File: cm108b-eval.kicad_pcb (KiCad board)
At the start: 2 copper layers, 60 x 50 mm, 42 parts, among them IC1 CM108B, J1 SPKR, J2 MIC, J3 RADIO_DATA, SW1 MUTE_REC, SW2 MUTE_PLAY, SW3 VOL_DN, SW4 VOL_UP

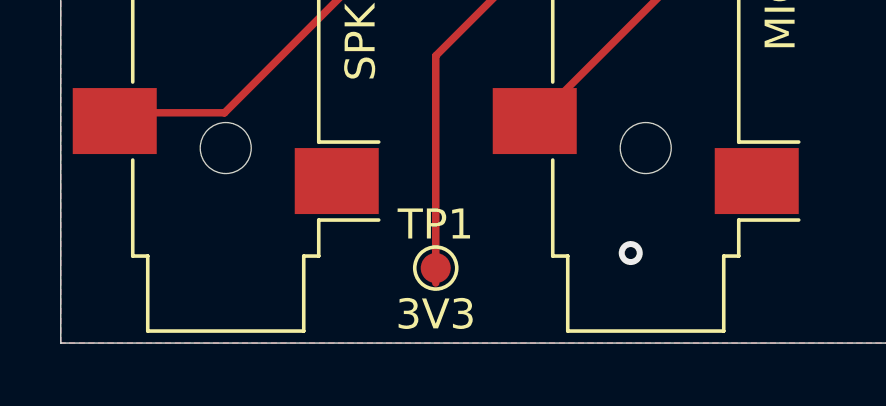
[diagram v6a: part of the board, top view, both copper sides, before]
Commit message: Fix USB connector from A to micro-B
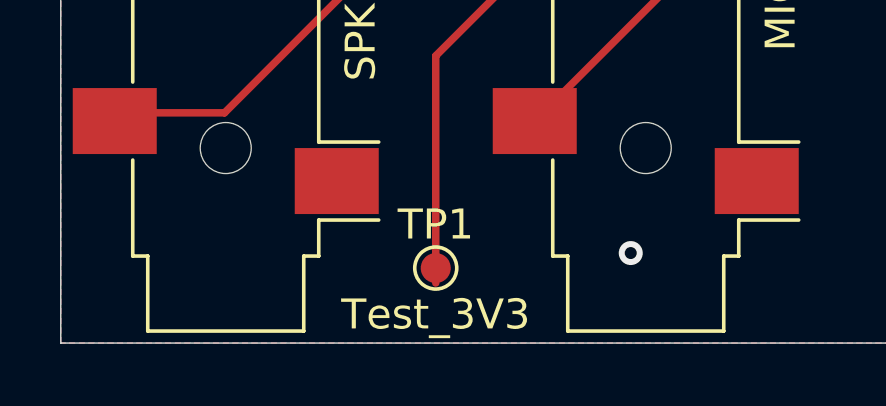
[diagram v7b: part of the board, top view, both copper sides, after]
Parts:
- JP2: value USB_A -> USB_MICRO_B
- TP1: value 3V3 -> Test_3V3
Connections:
- JP2 pad 4: GND -> (no net)
- JP2 pad 5: Net-(JP2-Pad5) -> GND
- JP2 pad 6: (no net) -> Net-(JP2-Pad6)
- L2 pad 2: Net-(JP2-Pad5) -> Net-(JP2-Pad6)

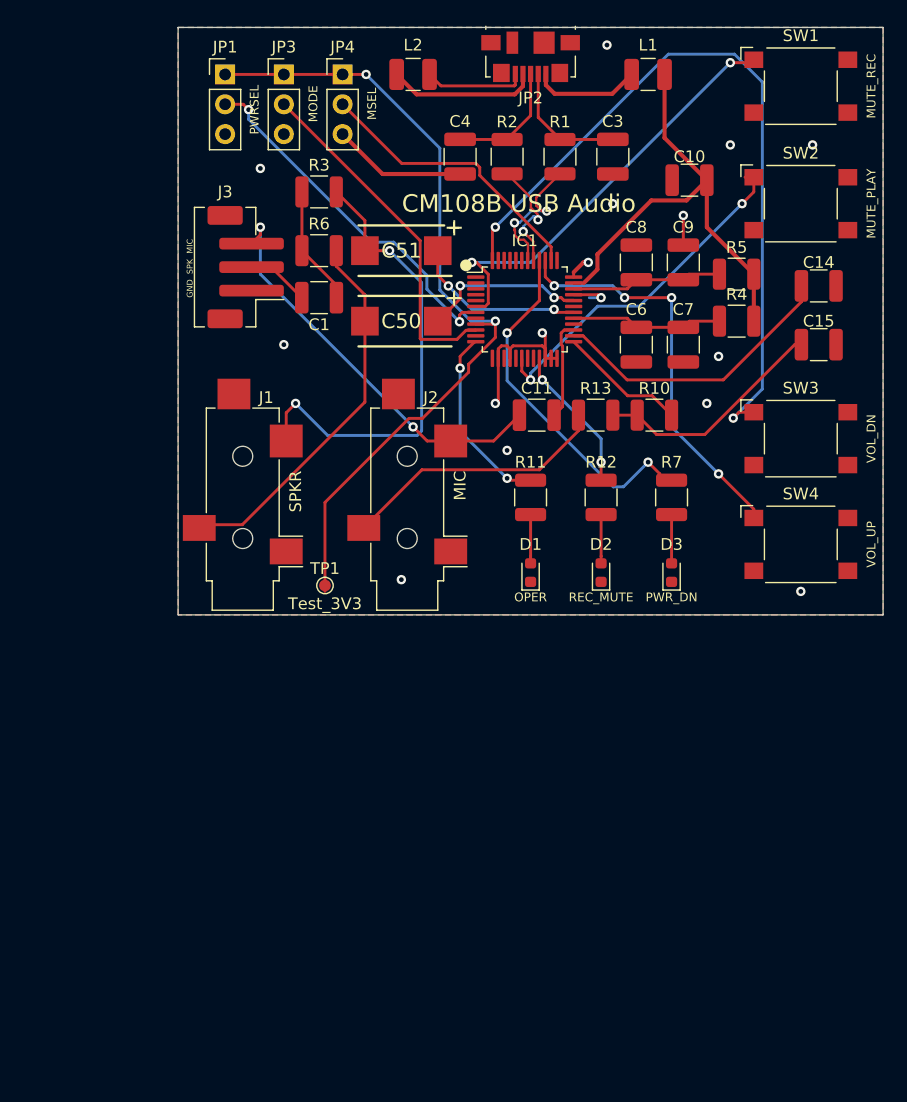
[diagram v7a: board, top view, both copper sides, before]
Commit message: Retool for JLCPCB assembly
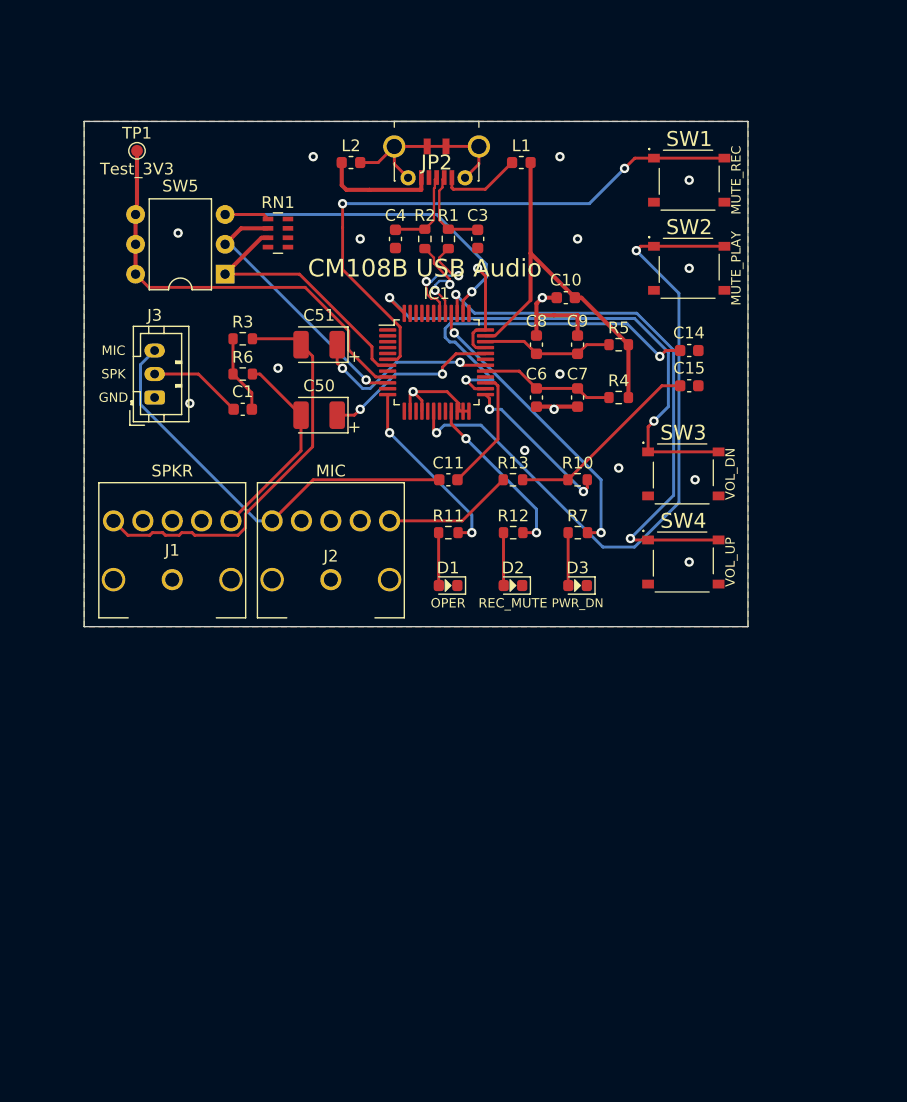
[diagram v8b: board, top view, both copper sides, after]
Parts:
- removed JP1: PWRSEL, Connector_PinHeader_2.54mm:PinHeader_1x03_P2.54mm_Vertical
- removed JP3: MODE, Connector_PinHeader_2.54mm:PinHeader_1x03_P2.54mm_Vertical
- removed JP4: MSEL, Connector_PinHeader_2.54mm:PinHeader_1x03_P2.54mm_Vertical
- added RN1: 10KΩ, Resistor_SMD:R_Array_Concave_4x0603, F.Cu at (138.5, 87.5)
- added SW5: SW_DIP_x03, Package_DIP:DIP-6_W7.62mm, F.Cu at (134.0, 91.0)
- C1, C10, C11, C14, C15, C3, C4, C6, C7, C8, C9: footprint Capacitor_SMD:C_1210_3225Metric -> Capacitor_SMD:C_0603_1608Metric
- C50, C51: footprint 293D477X9010E2TE3:CAPPM7343X430N -> Capacitor_Tantalum_SMD:CP_EIA-3528-21_Kemet-B
- J1, J2: footprint Connector_Audio:Jack_3.5mm_CUI_SJ-3524-SMT_Horizontal -> HRO Electronics:PJ-3900
- J3: footprint Connector_JST:JST_PH_B3B-PH-SM4-TB_1x03-1MP_P2.00mm_Vertical -> Connector_JST:JST_PH_B3B-PH-K_1x03_P2.00mm_Vertical
- JP2: footprint Connector_USB:USB_Micro-B_Molex_47346-0001 -> Shou_Han:MICROXNJ
- L1, L2: value L -> FerriteBead; footprint Inductor_SMD:L_1210_3225Metric -> Inductor_SMD:L_0603_1608Metric
- R1, R10, R11, R12, R13, R2, R3, R4, R5, R6, R7: footprint Resistor_SMD:R_1210_3225Metric -> Resistor_SMD:R_0603_1608Metric
- SW1, SW2, SW3, SW4: footprint Button_Switch_SMD:SW_SPST_Omron_B3FS-100xP -> XKB:TS1187ACCB
- moved TP1 40.3 mm to (126.5, 80.5)
- moved C10 14.5 mm to (163.0, 93.0)
- moved R3 14.1 mm to (135.5, 96.5)
- moved J3 13.5 mm to (128.0, 101.5)
- moved C3 13.5 mm to (155.5, 88.0)
- moved L1 13.1 mm to (159.2, 81.5)
- moved SW1 12.4 mm to (173.5, 83.0)
- moved R6 12.3 mm to (135.5, 99.5)
- moved C14 12.3 mm to (173.5, 97.5)
- moved R4 12.0 mm to (167.5, 101.5)
- moved R1 11.8 mm to (153.0, 88.0)
- moved R5 11.7 mm to (167.5, 97.0)
- moved C15 11.6 mm to (173.5, 100.5)
- moved C1 11.5 mm to (135.5, 102.5)
- moved C9 11.4 mm to (164.0, 97.0)
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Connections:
- net Net-(C3-Pad1) renamed /DJ-
- net Net-(C4-Pad1) renamed /DJ+
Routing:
- net +3V3: track 70.2 -> 36.6 mm, vias 2 -> 0
- net /MUTEP: track 30.1 -> 59.3 mm
- net /VOLDN: track 64.6 -> 42.7 mm
- net Net-(JP2-Pad6): track 0.00 -> 17.0 mm
- net /AUDIO_L: track 32.8 -> 17.1 mm
- net /MUTER: track 36.6 -> 50.3 mm
- net /VOLUP: track 34.8 -> 47.3 mm, vias 4 -> 2
- net /MIC_BIAS: track 23.0 -> 11.1 mm
- net Net-(JP2-Pad5): track 8.67 -> 0.00 mm
- net /MSEL: track 24.3 -> 32.8 mm, vias 0 -> 1
- net /PWRSEL: track 30.8 -> 22.6 mm, vias 2 -> 0
- net Net-(C14-Pad2): track 25.0 -> 32.1 mm, vias 0 -> 2
- net VBUS: track 39.9 -> 32.9 mm
- net /MODE: track 29.8 -> 22.9 mm, vias 0 -> 1
- net /AUDIO_R: track 40.6 -> 35.1 mm, vias 2 -> 0
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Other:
- board size 60 x 50 mm -> 56.5 x 43 mm
- board text added: "CM108B Audio Evaluation Board J1 C. Keller 2021-04-09"
- board text removed: "+"
- board text removed: "CM108B Audio Evaluation Board v3 C. Keller 2021-04-05"
- board text removed: "GND SPK MIC"
